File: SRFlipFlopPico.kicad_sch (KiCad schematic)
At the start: 9 parts, among them U1 74LS01, U2 TLV2462

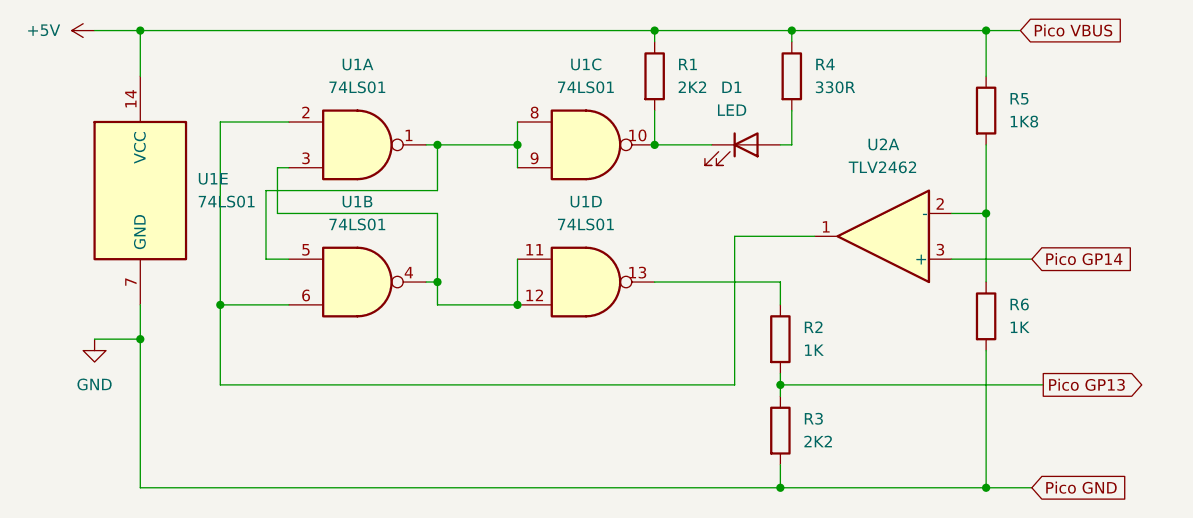
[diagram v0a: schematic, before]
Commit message: Added missing R7 pull-up on Pico output
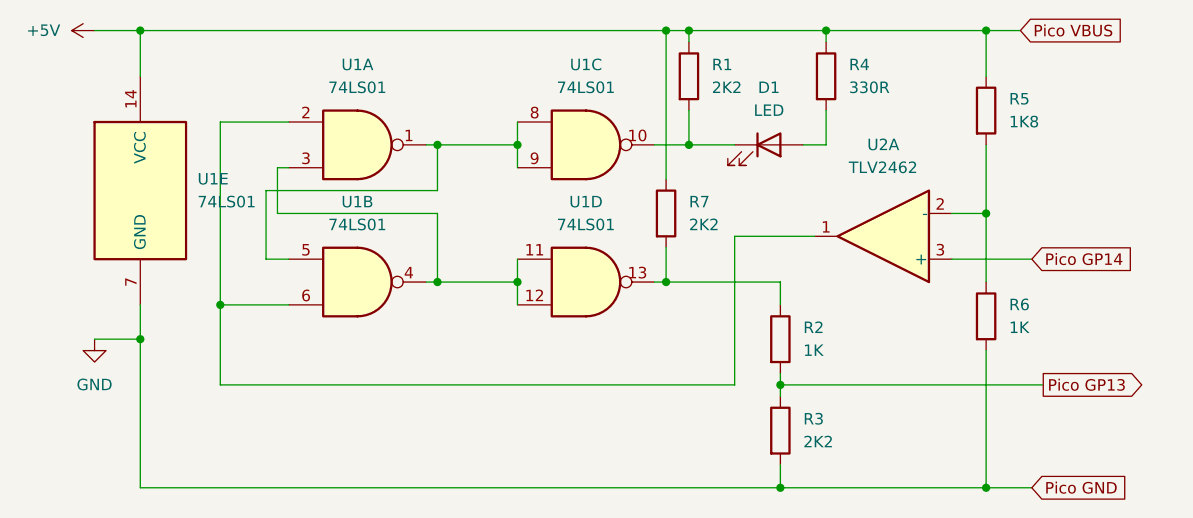
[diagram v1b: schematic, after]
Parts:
- added R7: 2K2, symbol Device:R
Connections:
- net +5V: now also R7.1
- net at R2.1, U1.13: now also R7.2
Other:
- moved on the sheet: D1, R1, R4
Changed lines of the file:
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@@
   (junction (at 35.56 20.32) (diameter 0) (color 0 0 0 0)
   )
+  (junction (at 68.58 48.26) (diameter 0) (color 0 0 0 0)
+  )
   (junction (at 106.68 59.69) (diameter 0) (color 0 0 0 0)
   )
-  (junction (at 68.58 48.26) (diameter 0) (color 0 0 0 0)
-  )
-  (junction (at 77.47 50.8) (diameter 0) (color 0 0 0 0)
+  (junction (at 111.76 20.32) (diameter 0) (color 0 0 0 0)
+  )
+  (junction (at 93.98 48.26) (diameter 0) (color 0 0 0 0)
+  )
+  (junction (at 93.98 20.32) (diameter 0) (color 0 0 0 0)
   )
   (junction (at 129.54 40.64) (diameter 0) (color 0 0 0 0)
@@
   (junction (at 68.58 33.02) (diameter 0) (color 0 0 0 0)
   )
+  (junction (at 77.47 48.26) (diameter 0) (color 0 0 0 0)
+  )
+  (junction (at 96.52 33.02) (diameter 0) (color 0 0 0 0)
+  )
   (junction (at 77.47 33.02) (diameter 0) (color 0 0 0 0)
   )
-  (junction (at 92.71 33.02) (diameter 0) (color 0 0 0 0)
-  )
   (junction (at 129.54 20.32) (diameter 0) (color 0 0 0 0)
   )
   (junction (at 44.45 50.8) (diameter 0) (color 0 0 0 0)
   )
-  (junction (at 107.95 20.32) (diameter 0) (color 0 0 0 0)
-  )
   (junction (at 35.56 54.61) (diameter 0) (color 0 0 0 0)
   )
-  (junction (at 92.71 20.32) (diameter 0) (color 0 0 0 0)
+  (junction (at 96.52 20.32) (diameter 0) (color 0 0 0 0)
   )
   (wire (pts (xy 44.45 50.8) (xy 52.07 50.8))
@@
     (stroke (width 0) (type default))
   )
-  (wire (pts (xy 92.71 20.32) (xy 92.71 21.59))
+  (wire (pts (xy 96.52 33.02) (xy 101.6 33.02))
+    (stroke (width 0) (type default))
+  )
+  (wire (pts (xy 96.52 20.32) (xy 96.52 21.59))
     (stroke (width 0) (type default))
   )
@@
     (stroke (width 0) (type default))
   )
-  (wire (pts (xy 68.58 50.8) (xy 68.58 48.26))
+  (wire (pts (xy 92.71 33.02) (xy 96.52 33.02))
     (stroke (width 0) (type default))
   )
@@
     (stroke (width 0) (type default))
   )
-  (wire (pts (xy 107.95 29.21) (xy 107.95 33.02))
+  (wire (pts (xy 111.76 29.21) (xy 111.76 33.02))
+    (stroke (width 0) (type default))
+  )
+  (wire (pts (xy 111.76 20.32) (xy 129.54 20.32))
     (stroke (width 0) (type default))
   )
@@
     (stroke (width 0) (type default))
   )
-  (wire (pts (xy 68.58 50.8) (xy 77.47 50.8))
-    (stroke (width 0) (type default))
-  )
   (wire (pts (xy 67.31 33.02) (xy 68.58 33.02))
     (stroke (width 0) (type default))
@@
     (stroke (width 0) (type default))
   )
-  (wire (pts (xy 92.71 33.02) (xy 99.06 33.02))
+  (wire (pts (xy 77.47 48.26) (xy 77.47 50.8))
     (stroke (width 0) (type default))
   )
@@
     (stroke (width 0) (type default))
   )
-  (wire (pts (xy 92.71 48.26) (xy 106.68 48.26))
+  (wire (pts (xy 92.71 48.26) (xy 93.98 48.26))
+    (stroke (width 0) (type default))
+  )
+  (wire (pts (xy 96.52 20.32) (xy 111.76 20.32))
+    (stroke (width 0) (type default))
+  )
+  (wire (pts (xy 96.52 29.21) (xy 96.52 33.02))
     (stroke (width 0) (type default))
   )
@@
     (stroke (width 0) (type default))
   )
-  (wire (pts (xy 92.71 20.32) (xy 107.95 20.32))
+  (wire (pts (xy 93.98 48.26) (xy 106.68 48.26))
     (stroke (width 0) (type default))
   )
@@
     (stroke (width 0) (type default))
   )
+  (wire (pts (xy 93.98 44.45) (xy 93.98 48.26))
+    (stroke (width 0) (type default))
+  )
   (wire (pts (xy 49.53 45.72) (xy 52.07 45.72))
     (stroke (width 0) (type default))
@@
     (stroke (width 0) (type default))
   )
-  (wire (pts (xy 106.68 33.02) (xy 107.95 33.02))
+  (wire (pts (xy 109.22 33.02) (xy 111.76 33.02))
     (stroke (width 0) (type default))
   )
@@
     (stroke (width 0) (type default))
   )
-  (wire (pts (xy 77.47 45.72) (xy 77.47 50.8))
-    (stroke (width 0) (type default))
-  )
-  (wire (pts (xy 107.95 20.32) (xy 129.54 20.32))
+  (wire (pts (xy 77.47 45.72) (xy 77.47 48.26))
+    (stroke (width 0) (type default))
+  )
+  (wire (pts (xy 93.98 20.32) (xy 93.98 36.83))
     (stroke (width 0) (type default))
   )
@@
     (stroke (width 0) (type default))
   )
+  (wire (pts (xy 93.98 20.32) (xy 96.52 20.32))
+    (stroke (width 0) (type default))
+  )
   (wire (pts (xy 101.6 59.69) (xy 44.45 59.69))
     (stroke (width 0) (type default))
@@
     (stroke (width 0) (type default))
   )
-  (wire (pts (xy 92.71 29.21) (xy 92.71 33.02))
-    (stroke (width 0) (type default))
-  )
   (wire (pts (xy 68.58 40.64) (xy 50.8 40.64))
     (stroke (width 0) (type default))
@@
     (stroke (width 0) (type default))
   )
-  (wire (pts (xy 35.56 20.32) (xy 92.71 20.32))
+  (wire (pts (xy 35.56 20.32) (xy 93.98 20.32))
+    (stroke (width 0) (type default))
+  )
+  (wire (pts (xy 68.58 48.26) (xy 77.47 48.26))
     (stroke (width 0) (type default))
   )
@@
     (stroke (width 0) (type default))
   )
-  (wire (pts (xy 107.95 20.32) (xy 107.95 21.59))
+  (wire (pts (xy 111.76 20.32) (xy 111.76 21.59))
     (stroke (width 0) (type default))
   )
@@
     )
   )
-  (symbol (lib_id "Device:R") (at 92.71 25.4 0) (unit 1)
+  (symbol (lib_id "Device:R") (at 96.52 25.4 0) (unit 1)
     (in_bom yes) (on_board yes) (dnp no)
-    (property "Reference" "R1" (at 95.25 24.13 0)
-      (effects (font (size 1.27 1.27)) (justify left))
-    )
-    (property "Value" "2K2" (at 95.25 26.67 0)
-      (effects (font (size 1.27 1.27)) (justify left))
-    )
-    (property "Footprint" "" (at 90.932 25.4 90)
-      (effects (font (size 1.27 1.27)) hide)
-    )
-    (property "Datasheet" "~" (at 92.71 25.4 0)
+    (property "Reference" "R1" (at 99.06 24.13 0)
+      (effects (font (size 1.27 1.27)) (justify left))
+    )
+    (property "Value" "2K2" (at 99.06 26.67 0)
+      (effects (font (size 1.27 1.27)) (justify left))
+    )
+    (property "Footprint" "" (at 94.742 25.4 90)
+      (effects (font (size 1.27 1.27)) hide)
+    )
+    (property "Datasheet" "~" (at 96.52 25.4 0)
       (effects (font (size 1.27 1.27)) hide)
     )
@@
         (path "/270eaa3d-97eb-451b-825c-edb2821b3ced"
           (reference "R6") (unit 1)
+        )
+      )
+    )
+  )
+  (symbol (lib_id "Device:R") (at 93.98 40.64 0) (unit 1)
+    (in_bom yes) (on_board yes) (dnp no) (fields_autoplaced)
+    (property "Reference" "R7" (at 96.52 39.37 0)
+      (effects (font (size 1.27 1.27)) (justify left))
+    )
+    (property "Value" "2K2" (at 96.52 41.91 0)
+      (effects (font (size 1.27 1.27)) (justify left))
+    )
+    (property "Footprint" "" (at 92.202 40.64 90)
+      (effects (font (size 1.27 1.27)) hide)
+    )
+    (property "Datasheet" "~" (at 93.98 40.64 0)
+      (effects (font (size 1.27 1.27)) hide)
+    )
+    (pin "1")
+    (pin "2")
+    (instances
+      (project "SRFlipFlopPico"
+        (path "/270eaa3d-97eb-451b-825c-edb2821b3ced"
+          (reference "R7") (unit 1)
         )
       )
@@
     )
   )
-  (symbol (lib_id "Device:LED") (at 102.87 33.02 0) (unit 1)
-    (in_bom yes) (on_board yes) (dnp no) (fields_autoplaced)
-    (property "Reference" "D1" (at 101.2825 26.67 0)
-      (effects (font (size 1.27 1.27)))
-    )
-    (property "Value" "LED" (at 101.2825 29.21 0)
-      (effects (font (size 1.27 1.27)))
-    )
-    (property "Footprint" "" (at 102.87 33.02 0)
-      (effects (font (size 1.27 1.27)) hide)
-    )
-    (property "Datasheet" "~" (at 102.87 33.02 0)
+  (symbol (lib_id "Device:LED") (at 105.41 33.02 0) (unit 1)
+    (in_bom yes) (on_board yes) (dnp no)
+    (property "Reference" "D1" (at 105.41 26.67 0)
+      (effects (font (size 1.27 1.27)))
+    )
+    (property "Value" "LED" (at 105.41 29.21 0)
+      (effects (font (size 1.27 1.27)))
+    )
+    (property "Footprint" "" (at 105.41 33.02 0)
+      (effects (font (size 1.27 1.27)) hide)
+    )
+    (property "Datasheet" "~" (at 105.41 33.02 0)
       (effects (font (size 1.27 1.27)) hide)
     )
@@
     )
   )
-  (symbol (lib_id "Device:R") (at 107.95 25.4 0) (unit 1)
-    (in_bom yes) (on_board yes) (dnp no) (fields_autoplaced)
-    (property "Reference" "R4" (at 110.49 24.13 0)
-      (effects (font (size 1.27 1.27)) (justify left))
-    )
-    (property "Value" "330R" (at 110.49 26.67 0)
-      (effects (font (size 1.27 1.27)) (justify left))
-    )
-    (property "Footprint" "" (at 106.172 25.4 90)
-      (effects (font (size 1.27 1.27)) hide)
-    )
-    (property "Datasheet" "~" (at 107.95 25.4 0)
-      (effects (font (size 1.27 1.27)) hide)
-    )
+  (symbol (lib_id "Device:R") (at 111.76 25.4 0) (unit 1)
+    (in_bom yes) (on_board yes) (dnp no) (fields_autoplaced)
+    (property "Reference" "R4" (at 114.3 24.13 0)
+      (effects (font (size 1.27 1.27)) (justify left))
+    )
+    (property "Value" "330R" (at 114.3 26.67 0)
+      (effects (font (size 1.27 1.27)) (justify left))
+    )
+    (property "Footprint" "" (at 109.982 25.4 90)
+      (effects (font (size 1.27 1.27)) hide)
+    )
+    (property "Datasheet" "~" (at 111.76 25.4 0)
+      (effects (font (size 1.27 1.27)) hide)
+    )
